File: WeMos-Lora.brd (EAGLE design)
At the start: 33.3 x 25.7 mm, 26 parts, among them P1 PADNORMAL, P2 PADNORMAL, P3 PADNORMAL, P4 PADNORMAL, U1 24AA02E64T

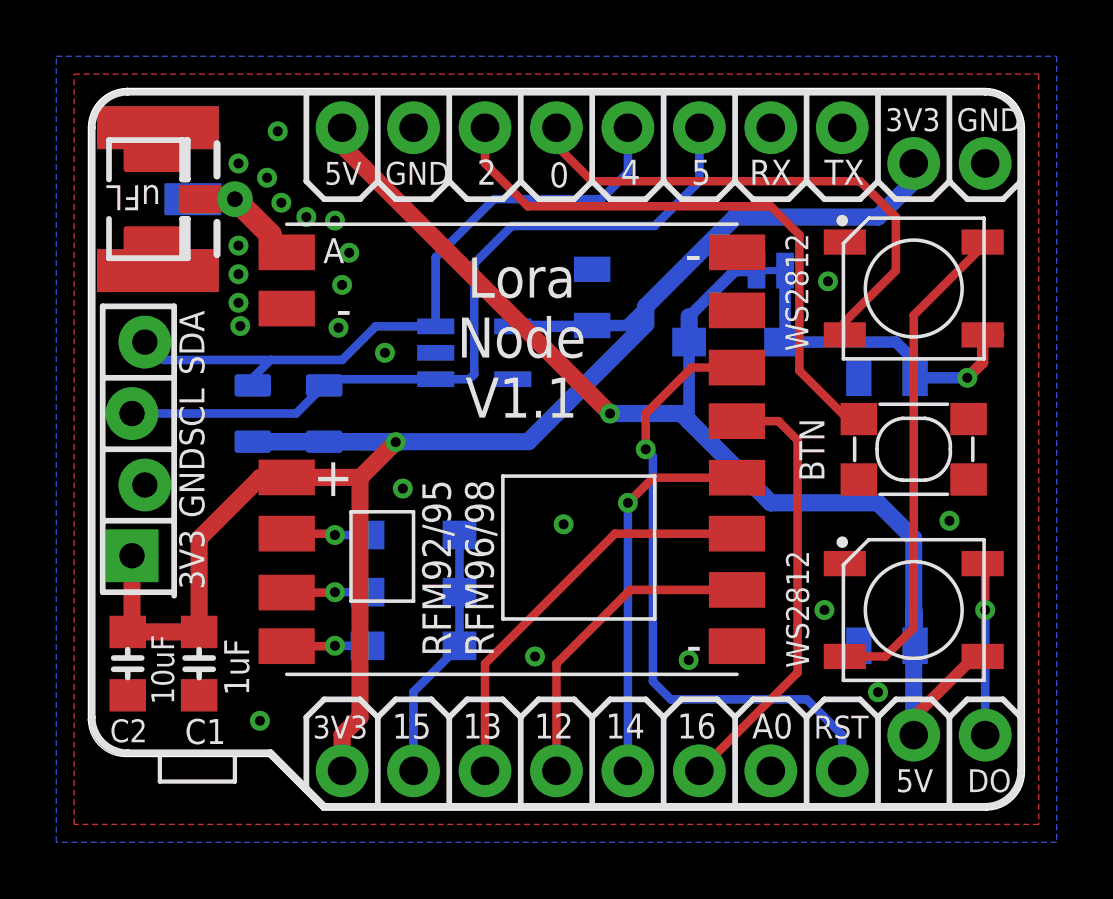
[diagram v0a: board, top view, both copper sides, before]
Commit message: * Removed LEDs + Switch * Freed GPIO16
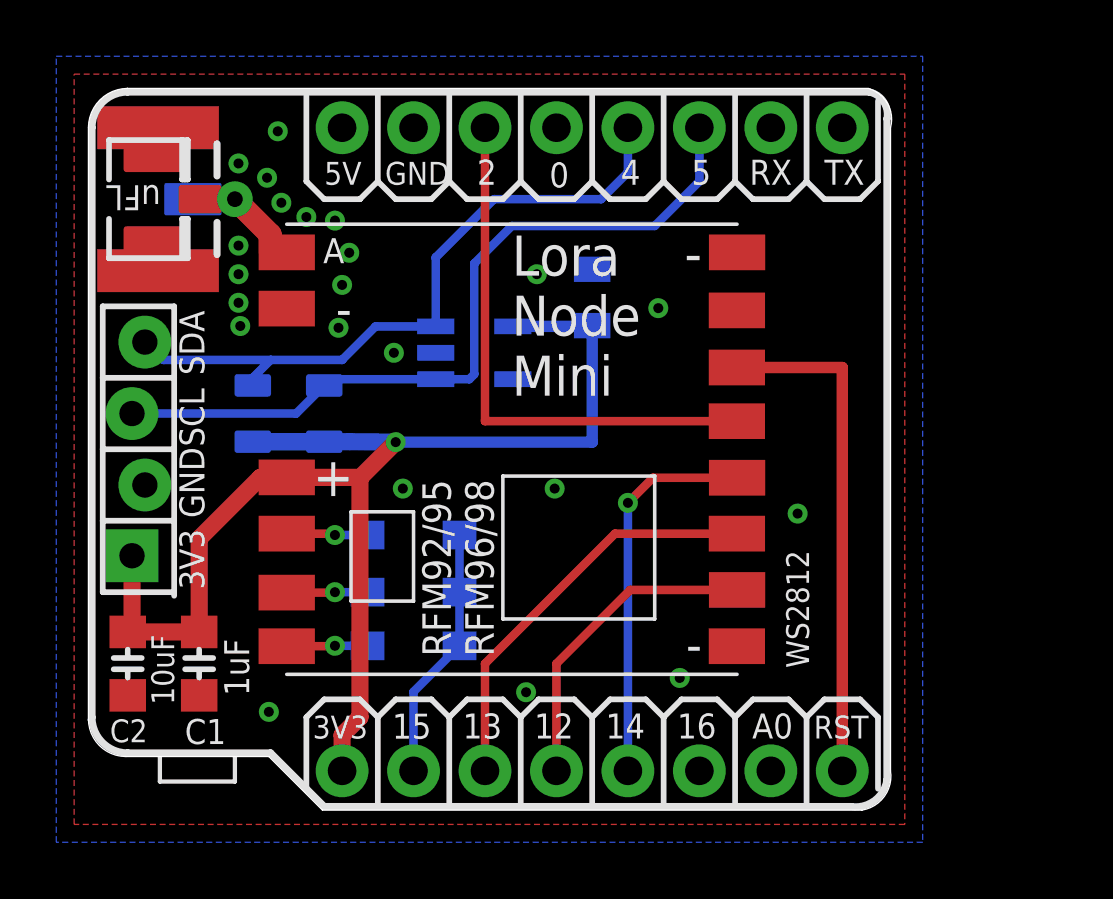
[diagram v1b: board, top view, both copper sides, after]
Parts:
- removed BTN: DHT-4235A, Switch-2016:SW4-SMD-4.2X3.2X2.5MM
- removed C3, C4: 100nF, _c2h:0805-CAP
- removed D1: 1N4148, Seeed-Discrete:SOD123-2.7X1.6
- removed JP4: JUMPER-PAD-2-NC_BY_TRACE, SparkFun-Passives:PAD-JUMPER-2-NC_BY_TRACE_YES_SILK
- removed P1, P2, P3, P4: PADNORMAL, _c2h:PAD
- removed U$4: (no value), _c2h:LOGO_CH2I_75MM
- removed WS1, WS2812: WS2812B, _c2h:WS2812B
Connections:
- removed net DO: P2.1, WS1.2
- removed net N$1: WS1.4, WS2812.2
- removed net VLED: C3.1, D1.2, JP4.1, WS2812.1
- net 3V3: no longer P4.1
- net 5V: no longer C4.1, D1.1, JP4.2, P1.1, WS1.1
- net GND: no longer BTN.3, C3.2, C4.2, P3.1, WS1.3, WS2812.3
- net GPIO0: no longer WS2812.4
- net GPIO16: no longer U$5.NSS
- net GPIO2: now also U$5.NSS; no longer BTN.1
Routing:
- net 5V: track 46.9 -> 0.00 mm, vias 1 -> 0
- net GPIO0: track 18.7 -> 0.00 mm
- net N$1: track 17.6 -> 0.00 mm
- net 3V3: track 66.1 -> 49.3 mm
- net GPIO16: track 15.6 -> 0.00 mm
- net VLED: track 12.3 -> 0.00 mm, vias 1 -> 0
- net DO: track 6.13 -> 0.00 mm, vias 1 -> 0
- net RST: track 22.3 -> 18.1 mm, vias 1 -> 0
- net GPIO2: track 21.2 -> 19.4 mm
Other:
- board size 33.3 x 25.7 mm -> 28.6 x 25.7 mm
- board text added: "CN V1"
- board text added: "Lora Node Mini"
- board text removed: "Cut Wire if you put D1 to avoid LED pb"
- board text removed: "DO"
- board text removed: "Lora Node"
- board text removed: "Lora Node V1.1"

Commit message: Removed display connector
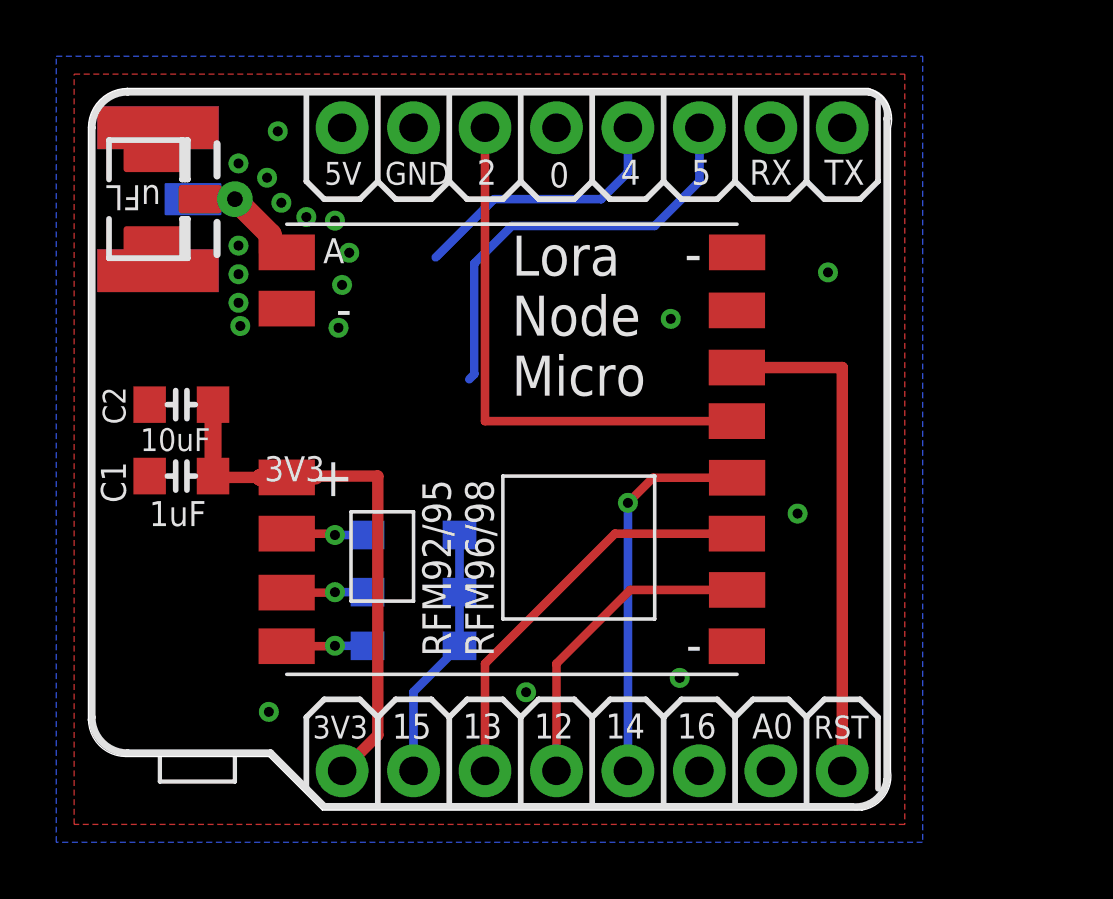
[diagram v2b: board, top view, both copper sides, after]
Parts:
- removed C5: 100nF, _c2h:0805-CAP
- removed I2C_OLED: CON_HEADER_1X04'LOCK', _c2h:1X04_LOCK
- removed R1, R2: 4.7K, _c2h:0805-RES
- removed U1: 24AA02E64T, Microchip-24AA02E64T:SOT95P270X145-5N
- moved C2 9.40 mm to (6.35, 14.3), turned to 0 degrees
- moved C1 6.70 mm to (6.35, 11.7), turned to 0 degrees
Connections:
- net 3V3: no longer C5.1, I2C_OLED.1, R1.2, R2.2, U1.4
- net GND: no longer C5.2, I2C_OLED.2, U1.2
- net SCL: no longer I2C_OLED.3, R2.1, U1.1
- net SDA: no longer I2C_OLED.4, R1.1, U1.3
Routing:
- net 3V3: track 49.3 -> 22.4 mm, vias 1 -> 0
- net SDA: track 24.4 -> 9.67 mm
- net SCL: track 27.8 -> 15.3 mm
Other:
- board text added: "Lora Node Micro"
- board text removed: "I2C PUP"
- board text removed: "Lora Node Mini"
- board text removed: "SCL"
- board text removed: "SDA"
- board text removed: "WS2812"
